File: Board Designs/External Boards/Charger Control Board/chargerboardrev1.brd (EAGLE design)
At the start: 54.1 x 41.6 mm, 20 parts, among them J1 JUMPER.1, X1 CONNECTOR-6NANO-FIT_VERTICAL-6, X3 CONNECTOR-2, X4 CONNECTOR-2

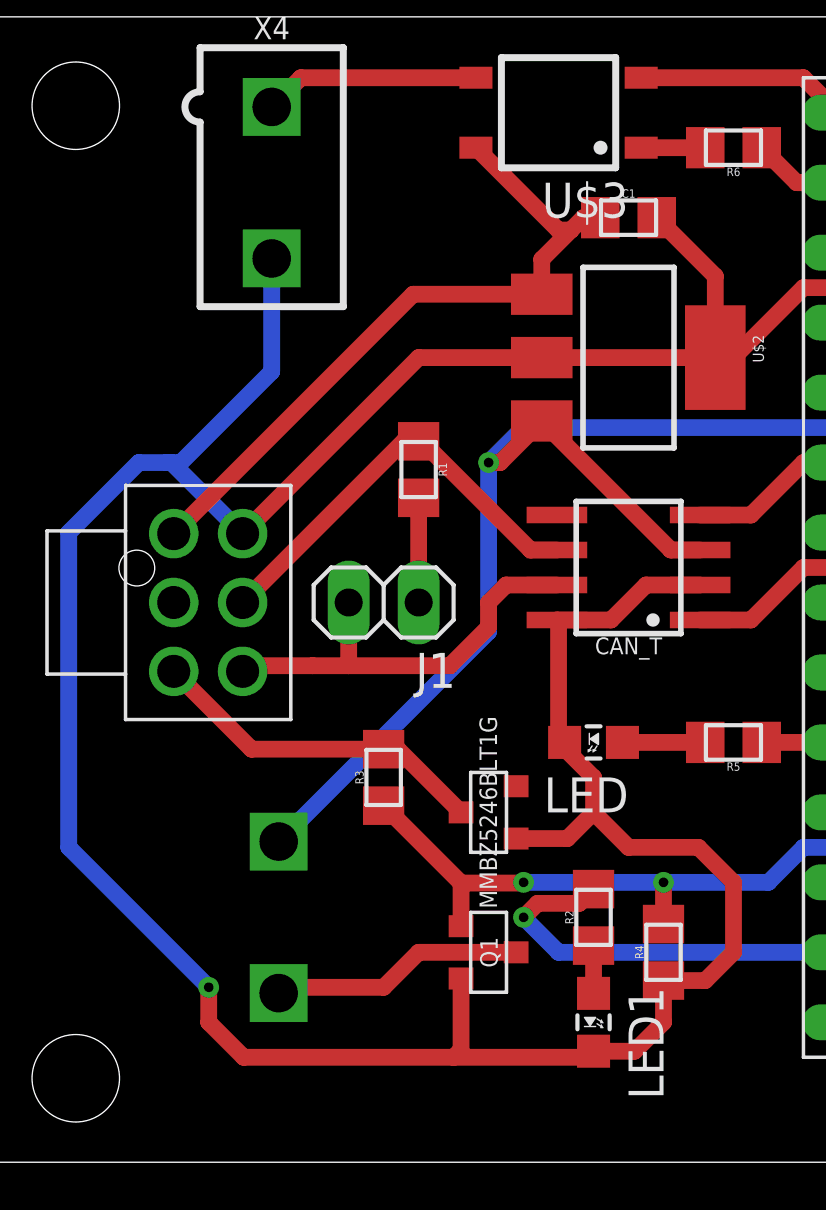
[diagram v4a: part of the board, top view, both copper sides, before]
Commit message: Modified charger board silkscreens for manufacturing
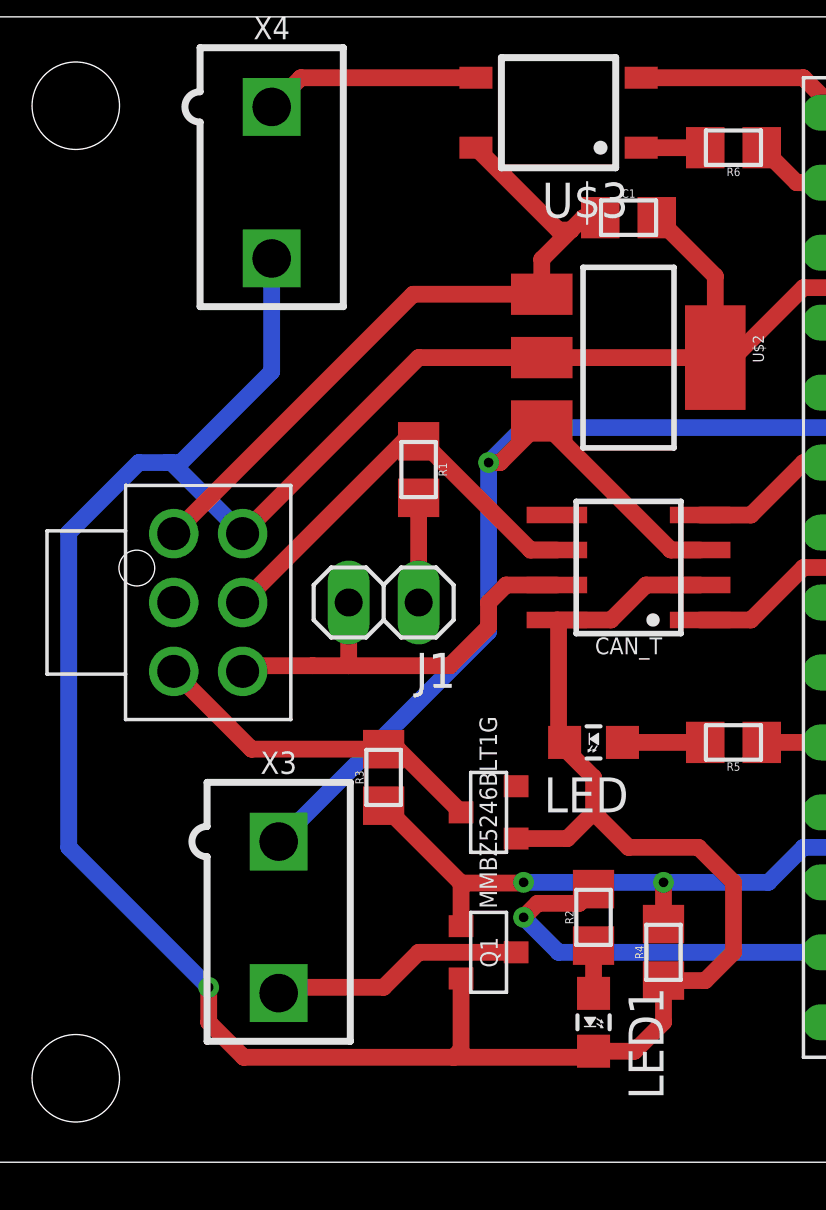
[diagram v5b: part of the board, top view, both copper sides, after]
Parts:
- flipped X3 to the top
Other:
- board text added: "CHARGE ENABLE"
- board text added: "POWER SWITCH"
